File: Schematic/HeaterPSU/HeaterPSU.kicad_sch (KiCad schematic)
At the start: 55 parts, among them J201 To MCU Board, J202 SMPS2_SEC, J203 Heater Output, Q201 IRF4905, Q202 BC847, Q203 BC847, Q204 BC857, Q205 IRF4905, SW201 SW_Rotary_1P5T_ALPSALPINE_SRBV, U201 L78L12_SOT89, U202 TPS54302

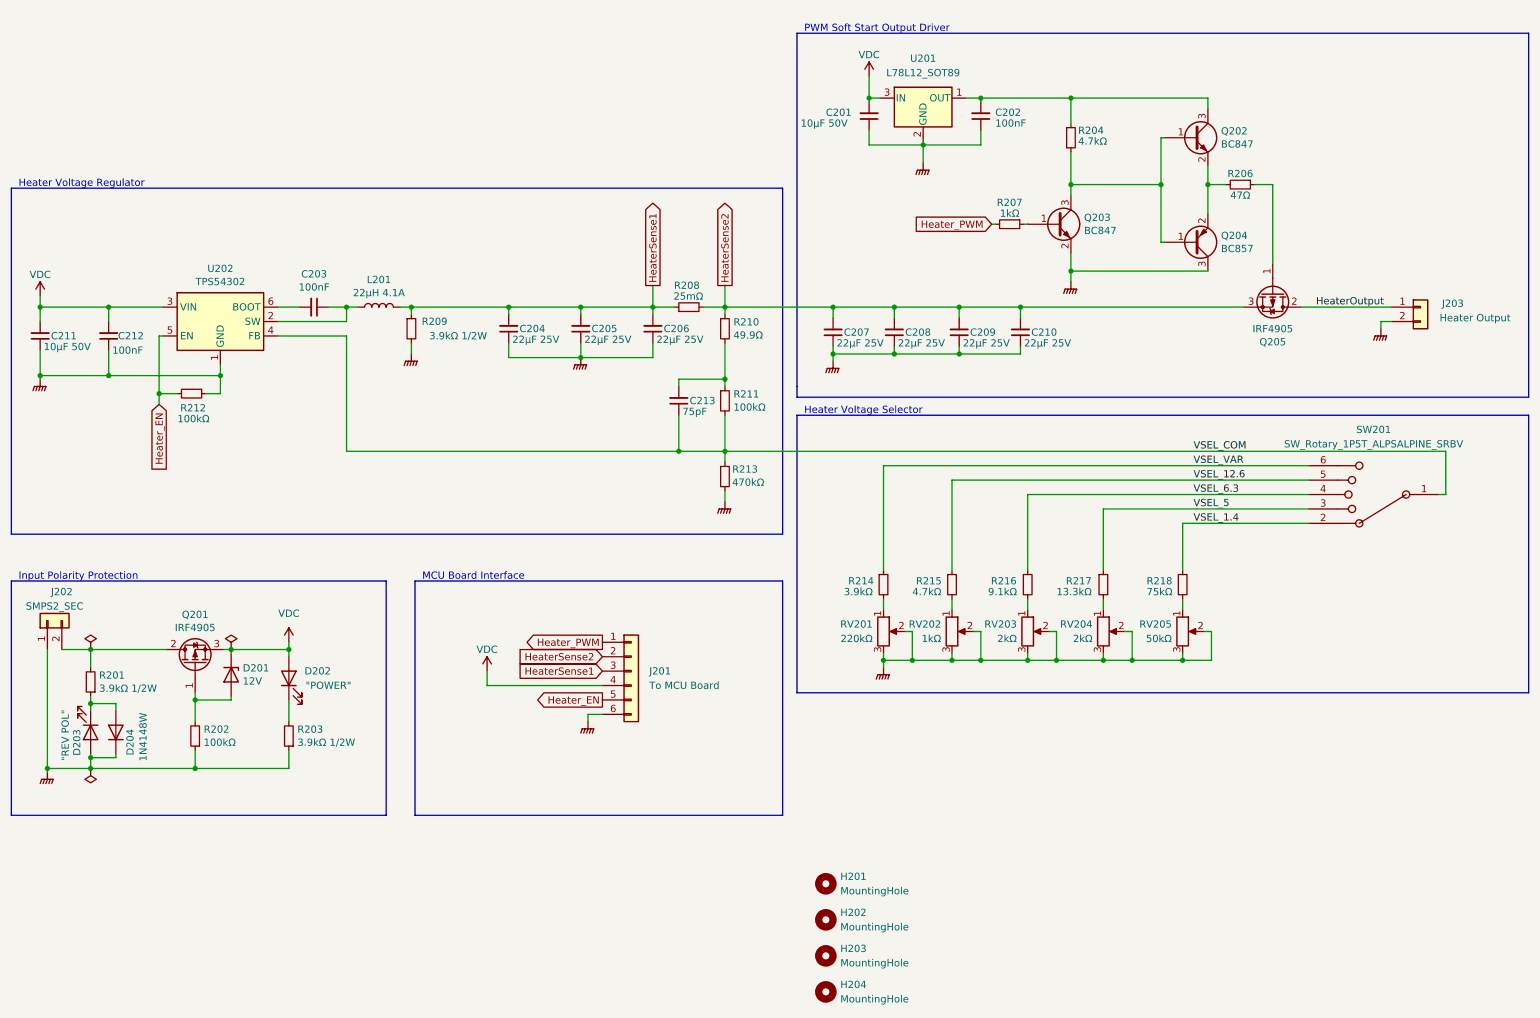
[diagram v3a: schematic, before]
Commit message: New PSU based on XL4005
Added current limiter
Added interface to uTracer PIC
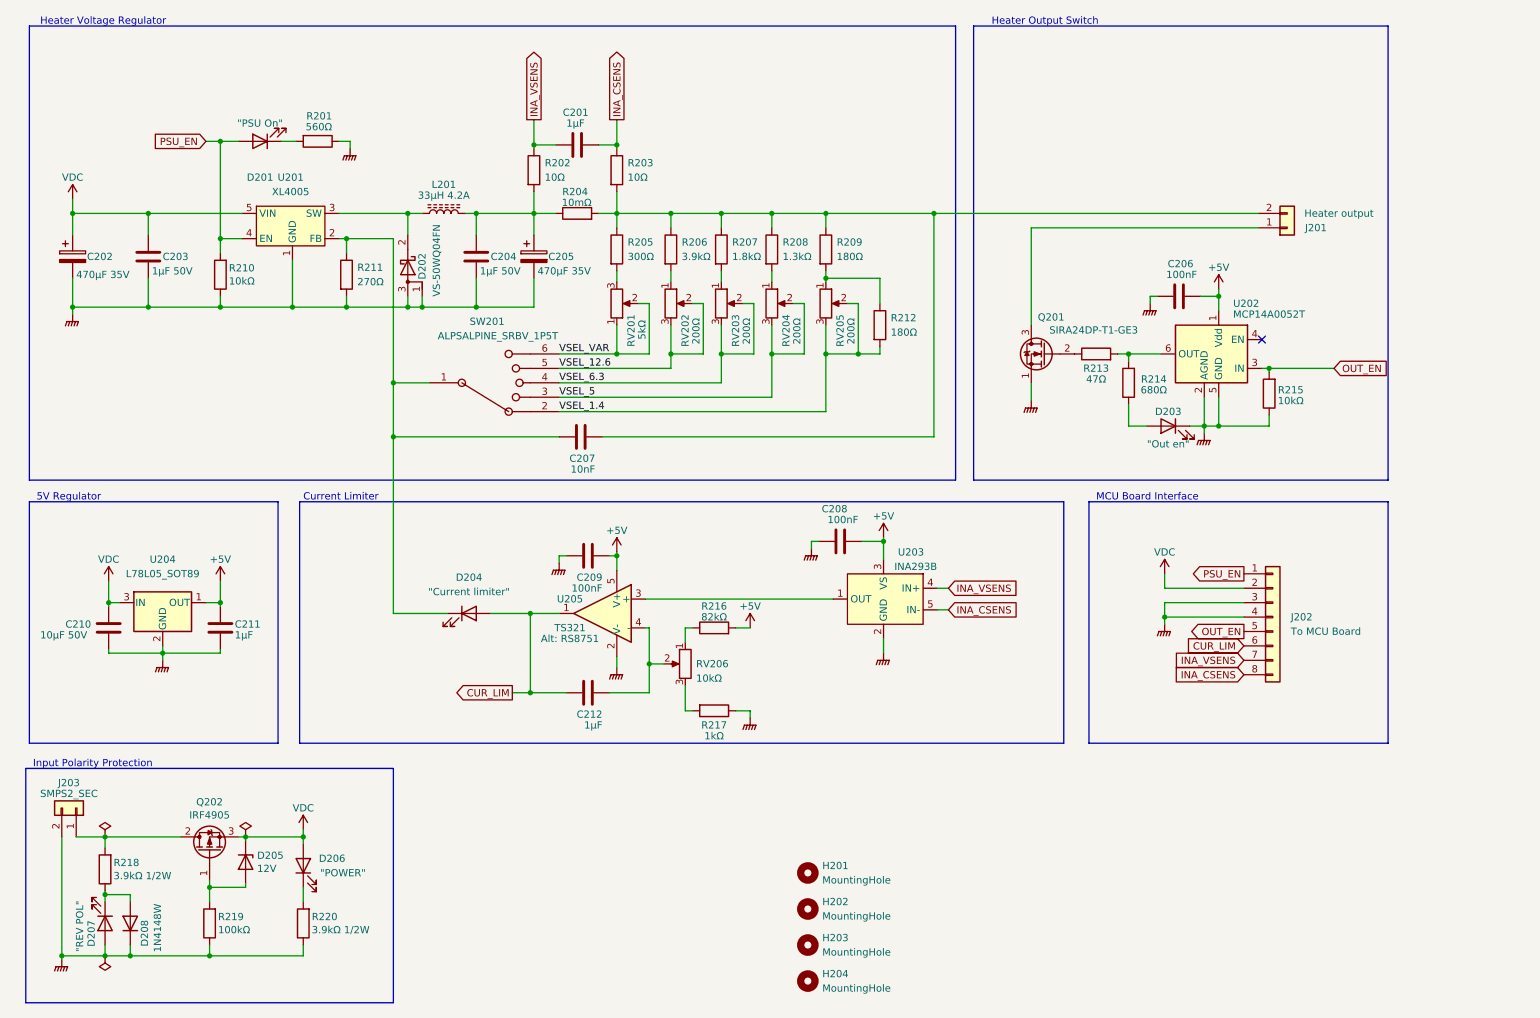
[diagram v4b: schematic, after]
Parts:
- removed C203, C212: 100nF, Capacitor_SMD:C_0805_2012Metric_Pad1.18x1.45mm_HandSolder, symbol Device:C_Small
- removed C204, C205, C206, C207, C208, C209, C210: 22µF 25V, Capacitor_SMD:C_0805_2012Metric_Pad1.18x1.45mm_HandSolder, symbol Device:C_Small
- removed C211: 10µF 50V, Capacitor_SMD:C_0805_2012Metric_Pad1.18x1.45mm_HandSolder, symbol Device:C_Small
- removed C213: 75pF, Capacitor_SMD:C_0805_2012Metric_Pad1.18x1.45mm_HandSolder, symbol Device:C_Small
- removed L201: 22µH 4.1A, Inductor_SMD:L_Wuerth_HCI-1040, symbol Device:L
- removed Q202, Q203: BC847, Package_TO_SOT_SMD:SOT-23, symbol Transistor_BJT:BC847
- removed Q204: BC857, Package_TO_SOT_SMD:SOT-23, symbol Transistor_BJT:BC857
- removed Q205: IRF4905, Package_TO_SOT_SMD:TO-263-2, symbol Transistor_FET:IRF4905
- removed R204, R215: 4.7kΩ, Resistor_SMD:R_0805_2012Metric_Pad1.20x1.40mm_HandSolder, symbol Device:R_Small
- removed R206: 47Ω, Resistor_SMD:R_0805_2012Metric_Pad1.20x1.40mm_HandSolder, symbol Device:R_Small
- removed R207: 1kΩ, Resistor_SMD:R_0805_2012Metric_Pad1.20x1.40mm_HandSolder, symbol Device:R_Small
- removed R209: 3.9kΩ 1/2W, Resistor_SMD:R_1210_3225Metric_Pad1.30x2.65mm_HandSolder, symbol Device:R_Small
- removed R210: 49.9Ω, Resistor_SMD:R_0805_2012Metric_Pad1.20x1.40mm_HandSolder, symbol Device:R_Small
- removed R211, R212: 100kΩ, Resistor_SMD:R_0805_2012Metric_Pad1.20x1.40mm_HandSolder, symbol Device:R_Small
- removed R213: 470kΩ, Resistor_SMD:R_0805_2012Metric_Pad1.20x1.40mm_HandSolder, symbol Device:R_Small
- removed R214: 3.9kΩ, Resistor_SMD:R_0805_2012Metric_Pad1.20x1.40mm_HandSolder, symbol Device:R_Small
- removed R216: 9.1kΩ, Resistor_SMD:R_0805_2012Metric_Pad1.20x1.40mm_HandSolder, symbol Device:R_Small
- removed R217: 13.3kΩ, Resistor_SMD:R_0805_2012Metric_Pad1.20x1.40mm_HandSolder, symbol Device:R_Small
- removed R218: 75kΩ, Resistor_SMD:R_0805_2012Metric_Pad1.20x1.40mm_HandSolder, symbol Device:R_Small
- removed U201: L78L12_SOT89, Package_TO_SOT_SMD:SOT-89-3, symbol Regulator_Linear:L78L12_SOT89
- removed U202: TPS54302, Package_TO_SOT_SMD:SOT-23-6_Handsoldering, symbol Regulator_Switching:TPS54302
- added C201, C212: 1µF, Capacitor_SMD:C_0603_1608Metric_Pad1.08x0.95mm_HandSolder, symbol Device:C
- added C202, C205: 470µF 35V, Capacitor_SMD:CP_Elec_8x10, symbol Device:C_Polarized
- added C203, C204: 1µF 50V, Capacitor_SMD:C_0805_2012Metric_Pad1.18x1.45mm_HandSolder, symbol Device:C
- added C206, C208, C209: 100nF, Capacitor_SMD:C_0603_1608Metric_Pad1.08x0.95mm_HandSolder, symbol Device:C
- added C207: 10nF, Capacitor_SMD:C_0805_2012Metric_Pad1.18x1.45mm_HandSolder, symbol Device:C
- added D201: "PSU On", LED_SMD:LED_0805_2012Metric_Pad1.15x1.40mm_HandSolder, symbol Device:LED
- added D202: VS-50WQ04FN, Package_TO_SOT_SMD:TO-252-2, symbol myDevices:D_Schottky_VS-50WQ04FN
- added D203: "Out en", LED_SMD:LED_0805_2012Metric_Pad1.15x1.40mm_HandSolder, symbol Device:LED
- added D204: "Current limiter", LED_SMD:LED_0805_2012Metric_Pad1.15x1.40mm_HandSolder, symbol Device:LED
- added L201: 33µH 4.2A, Inductor_SMD:L_12x12mm_H8mm, symbol Device:L_Ferrite
- added Q201: SIRA24DP-T1-GE3, myDevices:SIRA24DP-T1-GE3, symbol myDevices:SIRA24DP-T1-GE3
- added R201: 560Ω, Resistor_SMD:R_0603_1608Metric_Pad0.98x0.95mm_HandSolder, symbol Device:R
- added R202, R203: 10Ω, Resistor_SMD:R_0805_2012Metric_Pad1.20x1.40mm_HandSolder, symbol Device:R
- added R205: 300Ω, Resistor_SMD:R_0805_2012Metric_Pad1.20x1.40mm_HandSolder, symbol Device:R
- added R206: 3.9kΩ, Resistor_SMD:R_0805_2012Metric_Pad1.20x1.40mm_HandSolder, symbol Device:R
- added R207: 1.8kΩ, Resistor_SMD:R_0805_2012Metric_Pad1.20x1.40mm_HandSolder, symbol Device:R
- added R208: 1.3kΩ, Resistor_SMD:R_0805_2012Metric_Pad1.20x1.40mm_HandSolder, symbol Device:R
- added R209, R212: 180Ω, Resistor_SMD:R_0805_2012Metric_Pad1.20x1.40mm_HandSolder, symbol Device:R
- added R210: 10kΩ, Resistor_SMD:R_0805_2012Metric_Pad1.20x1.40mm_HandSolder, symbol Device:R
- added R211: 270Ω, Resistor_SMD:R_0805_2012Metric_Pad1.20x1.40mm_HandSolder, symbol Device:R
- added R213: 47Ω, Resistor_SMD:R_0603_1608Metric_Pad0.98x0.95mm_HandSolder, symbol Device:R
- added R214: 680Ω, Resistor_SMD:R_0603_1608Metric_Pad0.98x0.95mm_HandSolder, symbol Device:R
- added R215: 10kΩ, Resistor_SMD:R_0603_1608Metric_Pad0.98x0.95mm_HandSolder, symbol Device:R
- added R216: 82kΩ, Resistor_SMD:R_0603_1608Metric_Pad0.98x0.95mm_HandSolder, symbol Device:R
- added R217: 1kΩ, Resistor_SMD:R_0603_1608Metric_Pad0.98x0.95mm_HandSolder, symbol Device:R
- added RV206: 10kΩ, Potentiometer_THT:Potentiometer_Bourns_PTV09A-1_Single_Vertical, symbol Device:R_Potentiometer
- added U201: XL4005, Package_TO_SOT_SMD:TO-263-5_TabPin3, symbol myDevices:XL4005
- added U202: MCP14A0052T, Package_TO_SOT_SMD:SOT-23-6_Handsoldering, symbol myDevices:MCP14A0052T
- added U203: INA293B, Package_TO_SOT_SMD:SOT-23-5_HandSoldering, symbol myDevices:INA293B
- added U204: L78L05_SOT89, Package_TO_SOT_SMD:SOT-89-3, symbol Regulator_Linear:L78L05_SOT89
- added U205: TS321, Package_TO_SOT_SMD:SOT-23-5_HandSoldering, symbol myDevices:RS8751
- C210: renamed from C201; footprint Capacitor_SMD:C_0805_2012Metric_Pad1.18x1.45mm_HandSolder -> Capacitor_SMD:C_0603_1608Metric_Pad1.08x0.95mm_HandSolder; symbol Device:C_Small -> Device:C
- C211: renamed from C202; value 100nF -> 1µF; footprint Capacitor_SMD:C_0805_2012Metric_Pad1.18x1.45mm_HandSolder -> Capacitor_SMD:C_0603_1608Metric_Pad1.08x0.95mm_HandSolder; symbol Device:C_Small -> Device:C
- J201: renamed from J202; value SMPS2_SEC -> Heater output
- J202: renamed from J201; footprint Connector_PinSocket_2.54mm:PinSocket_1x06_P2.54mm_Vertical -> Connector_PinSocket_2.54mm:PinSocket_1x08_P2.54mm_Vertical; symbol Connector_Generic:Conn_01x06 -> Connector_Generic:Conn_01x08
- J203: value Heater Output -> SMPS2_SEC
- R204: renamed from R208; value 25mΩ -> 10mΩ; symbol Device:R_Small -> Device:R
- R218: renamed from R201; symbol Device:R_Small -> Device:R
- R219: renamed from R202; symbol Device:R_Small -> Device:R
- R220: renamed from R203; symbol Device:R_Small -> Device:R
- RV201: value 220kΩ -> 5kΩ
- RV202: value 1kΩ -> 200Ω; footprint Potentiometer_THT:Potentiometer_Runtron_RM-065_Vertical -> Potentiometer_SMD:Potentiometer_TT_35W
- RV203, RV204: value 2kΩ -> 200Ω; footprint Potentiometer_THT:Potentiometer_Runtron_RM-065_Vertical -> Potentiometer_SMD:Potentiometer_TT_35W
- RV205: value 50kΩ -> 200Ω; footprint Potentiometer_THT:Potentiometer_Runtron_RM-065_Vertical -> Potentiometer_SMD:Potentiometer_TT_35W
- SW201: value SW_Rotary_1P5T_ALPSALPINE_SRBV -> ALPSALPINE_SRBV_1P5T
- renumbered D201 to D205, D202 to D206, D203 to D207, D204 to D208, Q201 to Q202
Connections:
- net HeaterOutput is gone; now on an unnamed net: J203.1 (Pin_1)
- net GNDPWR: now also J202.3 (Pin_3), J202.4 (Pin_4), C202.2, C203.2, C204.2, C205.2, C206.1, C208.1, C209.1, D202.1 (A), D202.3 (A), D203.1 (K), Q201.1 (S), R201.1, R210.1, R211.2, R215.1, R217.1, U201.1 (GND), U202.2 (AGND), U202.5 (GND), U203.2 (GND), U204.2 (GND), U205.2 (V-); no longer J201.1 (Pin_1), J202.6 (Pin_6), RV201.2, RV201.3, RV202.2, RV202.3, RV203.2, RV203.3, RV204.2, RV204.3, RV205.2, RV205.3
- net VDC: now also J202.2 (Pin_2), C202.1, C203.1, U201.5 (VIN), U204.3 (IN); no longer J202.4 (Pin_4)
- net VSEL_1.4: now also RV205.2, RV205.3, R212.2
- net VSEL_12.6: now also RV202.2, RV202.3
- net VSEL_5: now also RV204.2, RV204.3
- net VSEL_6.3: now also RV203.2, RV203.3
- net VSEL_VAR: now also RV201.1, RV201.2
- net +5V: now reaches C211.2
- net +5V: now also C206.2, C208.2, C209.2, R216.2, U202.1 (Vdd), U203.3 (VS), U204.1 (OUT), U205.5 (V+)
- net at RV204.1: now also R208.2
- net at RV202.1: now also R206.2
- net at RV203.1: now also R207.2
- net at Q202.2 (D), R218.2: no longer J201.2 (Pin_2)
- net at RV205.1: now also R209.2, R212.1
- net HeaterSense1: no longer names the net of R204.1
- net HeaterSense1: now also C204.1, C205.1, L201.2, R202.2; no longer J202.3 (Pin_3)
- net HeaterSense2: no longer names the net of R204.2
- net HeaterSense2: now also J201.2 (Pin_2), C207.2, R203.2, R205.1, R206.1, R207.1, R208.1, R209.1; no longer J202.2 (Pin_2)
- net Heater_EN renamed OUT_EN
- net OUT_EN: now also R215.2, U202.3 (IN)
- net Heater_PWM renamed PSU_EN
- net PSU_EN: now also D201.2 (A), R210.2, U201.4 (EN)
- net VSEL_COM: no longer names the net of SW201.1
- net VSEL_COM: now also C207.1, D204.1 (K), R211.1, U201.2 (FB)
- new net: D203.2 (A), R214.1
- new net: R213.2, R214.2, U202.6 (OUT)
- new net: U203.1 (OUT), U205.3 (+)
- new net: R205.2, RV201.3
- new net: D202.2 (K), L201.1, U201.3 (SW)
- new net: Q201.2 (G), R213.1
- new net: J201.1 (Pin_1), Q201.3 (D)
- new net: D201.1 (K), R201.2
- new net: R216.1, RV206.1
- new net: C212.2, RV206.2, U205.4 (-)
- new net: R217.2, RV206.3
- new net CUR_LIM: C212.1, D204.2 (A), J202.6 (Pin_6), U205.1
- new net INA_CSENS: C201.1, J202.8 (Pin_8), R203.1, U203.5 (IN-)
- new net INA_VSENS: C201.2, J202.7 (Pin_7), R202.1, U203.4 (IN+)
- no-connect marks 0 -> 1
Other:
- note added: "5V Regulator"
- note added: "Current Limiter"
- note added: "Heater Output Switch"
- note removed: "Heater Voltage Selector"
- note removed: "PWM Soft Start Output Driver"
- moved on the sheet: C210, C211, D205, D206, D207, D208, H201, H202, H203, H204, J201, Q202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

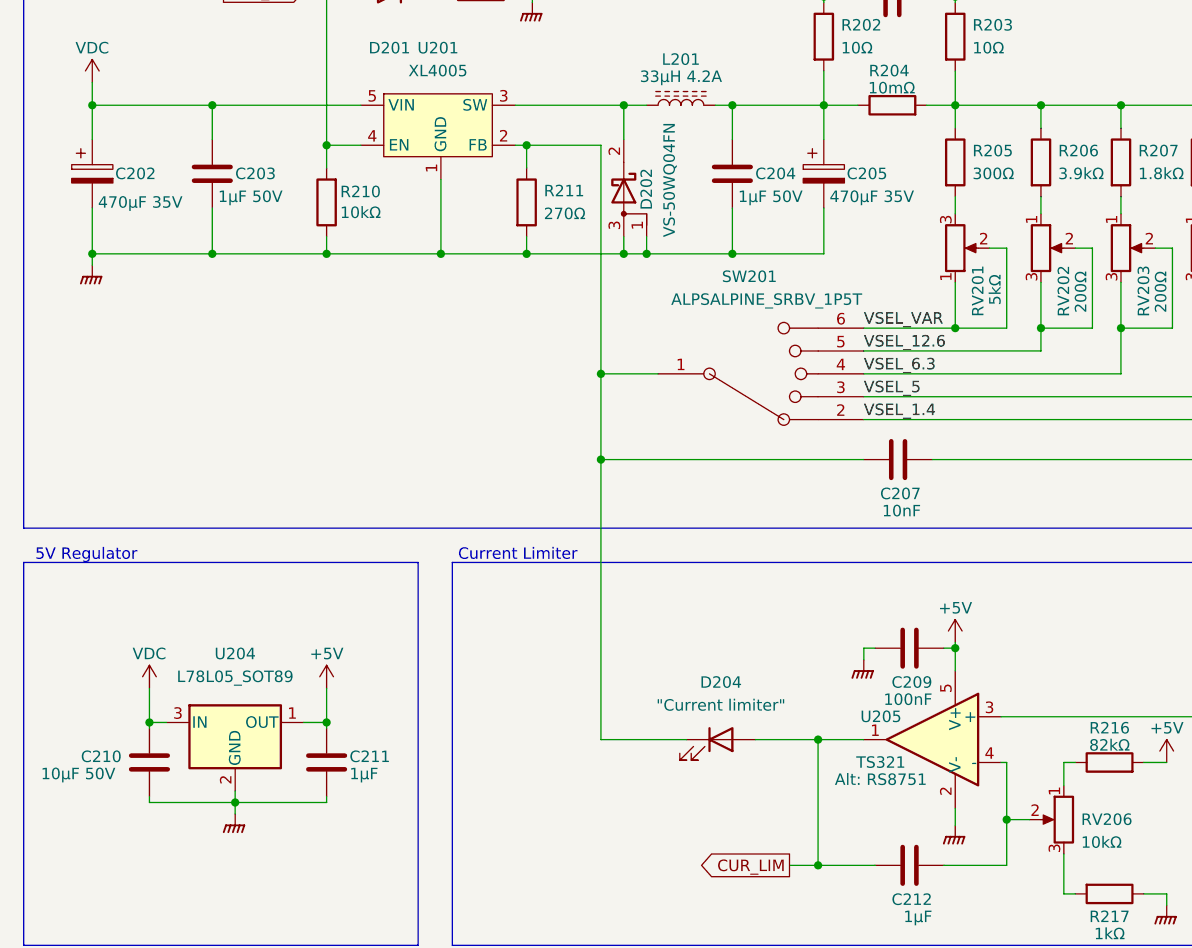
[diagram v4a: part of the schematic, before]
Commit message: Updated component values
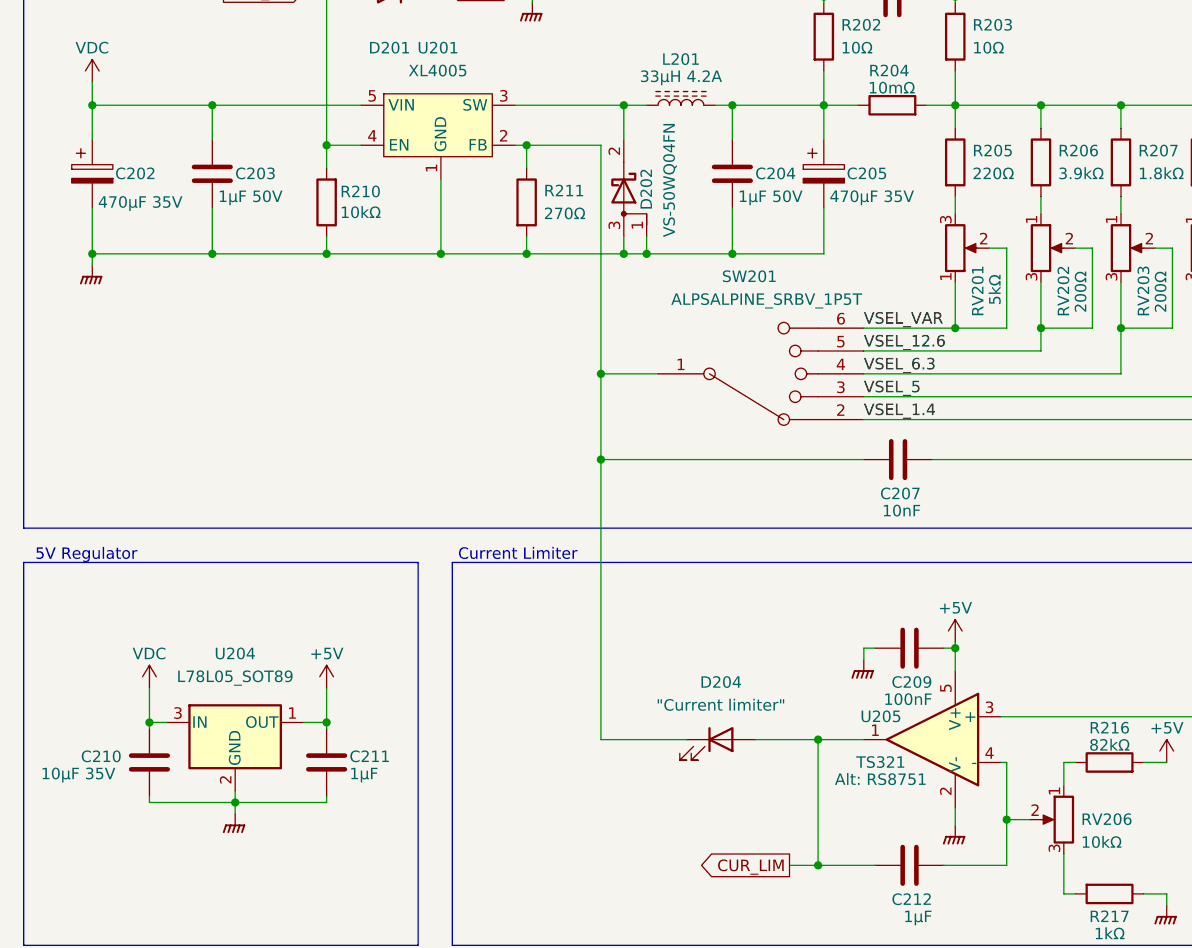
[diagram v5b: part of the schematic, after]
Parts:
- C210: value 10µF 50V -> 10µF 35V
- R205: value 300Ω -> 220Ω
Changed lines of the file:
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@@
       (effects (font (size 1.27 1.27)) (justify left))
     )
-    (property "Value" "300Ω" (id 1) (at 121.92 59.055 0)
+    (property "Value" "220Ω" (id 1) (at 121.92 59.055 0)
       (effects (font (size 1.27 1.27)) (justify left))
     )
@@
       (effects (font (size 1.27 1.27)) (justify right))
     )
-    (property "Value" "10µF 50V" (id 1) (at 18.415 125.73 0)
+    (property "Value" "10µF 35V" (id 1) (at 18.415 125.73 0)
       (effects (font (size 1.27 1.27)) (justify right))
     )
@@
     )
     (path "/bb18a299-7699-4466-9b2d-700e0d61665f"
-      (reference "C210") (unit 1) (value "10µF 50V") (footprint "Capacitor_SMD:C_0603_1608Metric_Pad1.08x0.95mm_HandSolder")
+      (reference "C210") (unit 1) (value "10µF 35V") (footprint "Capacitor_SMD:C_0603_1608Metric_Pad1.08x0.95mm_HandSolder")
     )
     (path "/fb83581e-89da-405d-81be-21921805dc14"
@@
     )
     (path "/acdc8974-c683-421f-9729-317698c4e535"
-      (reference "R205") (unit 1) (value "300Ω") (footprint "Resistor_SMD:R_0805_2012Metric_Pad1.20x1.40mm_HandSolder")
+      (reference "R205") (unit 1) (value "220Ω") (footprint "Resistor_SMD:R_0805_2012Metric_Pad1.20x1.40mm_HandSolder")
     )
     (path "/4ff606ef-3125-46e2-b957-680ff1671858"

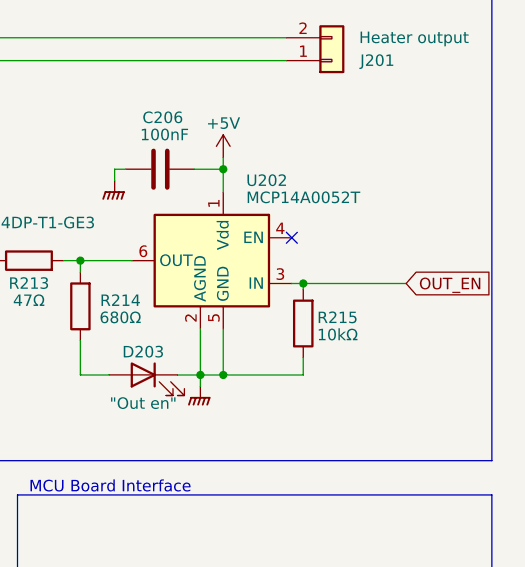
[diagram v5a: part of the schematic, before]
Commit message: Updated pin names
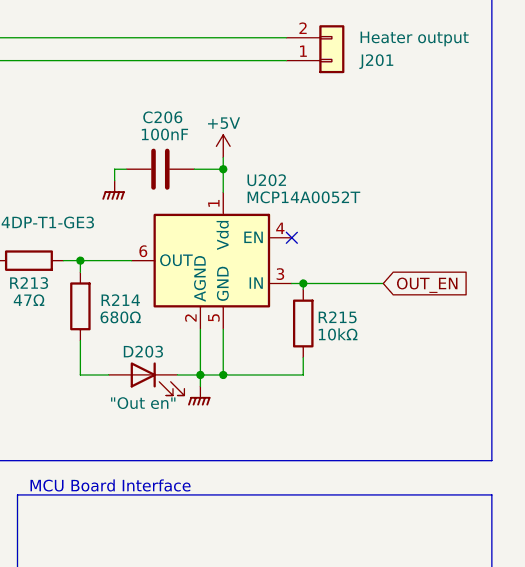
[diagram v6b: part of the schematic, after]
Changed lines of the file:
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@@
     (stroke (width 0) (type default) (color 0 0 0 0))
   )
-  (wire (pts (xy 234.95 78.74) (xy 246.38 78.74))
+  (wire (pts (xy 234.95 78.74) (xy 243.84 78.74))
     (stroke (width 0) (type default) (color 0 0 0 0))
   )
@@
     )
   )
-  (global_label "OUT_EN" (shape input) (at 246.38 78.74 0) (fields_autoplaced)
+  (global_label "OUT_EN" (shape input) (at 243.84 78.74 0) (fields_autoplaced)
     (effects (font (size 1.27 1.27)) (justify left))
-    (property "Intersheet References" "${INTERSHEET_REFS}" (id 0) (at 255.8688 78.6606 0)
+    (property "Intersheet References" "${INTERSHEET_REFS}" (id 0) (at 253.3288 78.6606 0)
       (effects (font (size 1.27 1.27)) (justify left) hide)
     )
